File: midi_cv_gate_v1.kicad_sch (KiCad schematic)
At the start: 29 parts, among them J1 Conn_02x05_Odd_Even, J34 Conn_01x08, J35 Conn_01x08, J36 Conn_01x20, J37 Conn_01x20, J42 Conn_01x20, J43 Conn_01x20, U1 LM7805_TO220

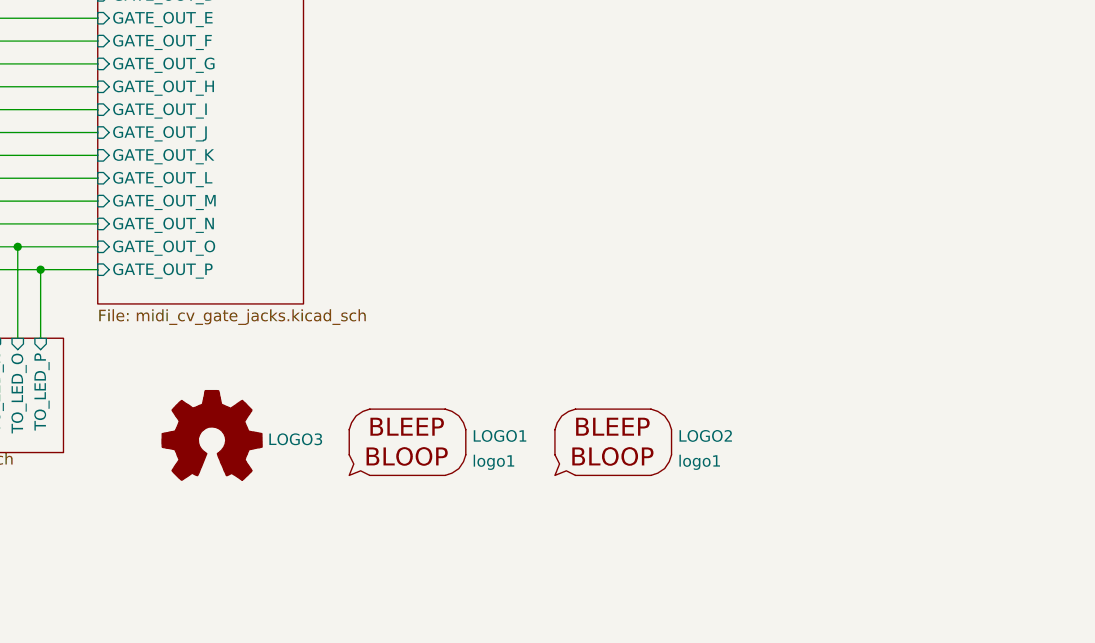
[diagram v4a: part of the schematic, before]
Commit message: First pass routing done, ERC passes, except interboard nets
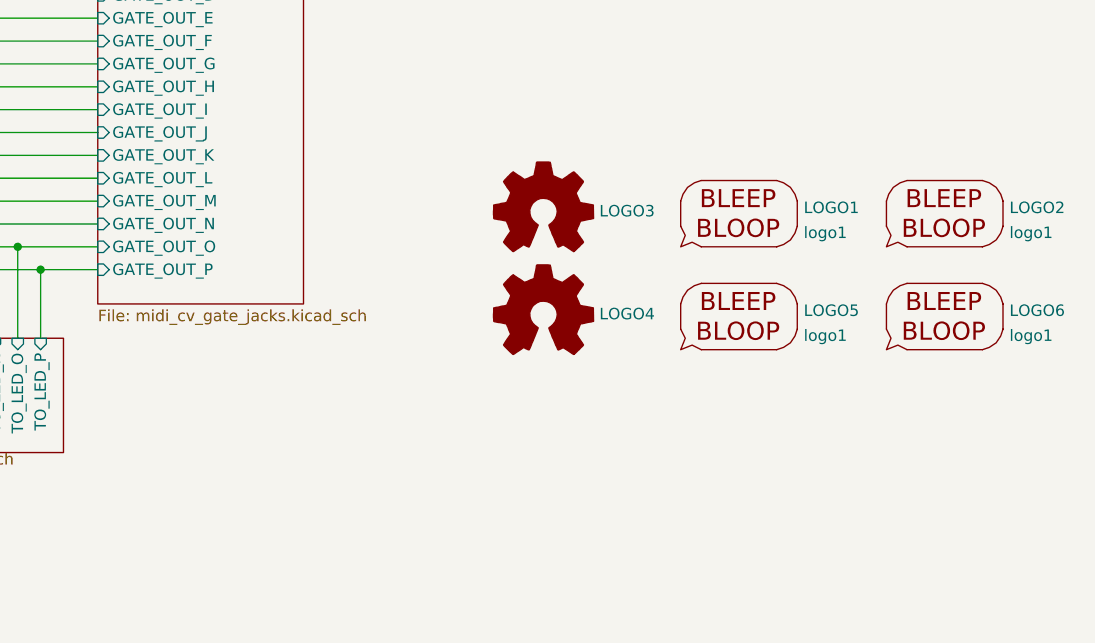
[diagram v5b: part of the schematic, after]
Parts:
- added LOGO4: Logo_Open_Hardware_Small, Symbol:OSHW-Symbol_6.7x6mm_SilkScreen, symbol My Stuff:Logo_Open_Hardware_Small
- added LOGO5: logo1, My Stuff:Logo1, symbol My Stuff:logo1
- added LOGO6: logo1, My Stuff:Logo2, symbol My Stuff:logo1
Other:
- moved on the sheet: LOGO1, LOGO2, LOGO3
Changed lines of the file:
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@@
     (pin "1")
   )
-  (symbol (lib_id "My Stuff:Logo_Open_Hardware_Small") (at 187.96 173.99 0) (unit 1)
-    (in_bom yes) (on_board yes) (fields_autoplaced)
-    (property "Reference" "LOGO3" (id 0) (at 194.1576 173.834 0)
-      (effects (font (size 1.27 1.27)) (justify left))
-    )
-    (property "Value" "Logo_Open_Hardware_Small" (id 1) (at 187.96 179.705 0)
-      (effects (font (size 1.27 1.27)) hide)
-    )
-    (property "Footprint" "Symbol:OSHW-Symbol_6.7x6mm_SilkScreen" (id 2) (at 187.96 173.99 0)
-      (effects (font (size 1.27 1.27)) hide)
-    )
-    (property "Datasheet" "~" (id 3) (at 187.96 173.99 0)
+  (symbol (lib_id "My Stuff:Logo_Open_Hardware_Small") (at 224.79 148.59 0) (unit 1)
+    (in_bom yes) (on_board yes) (fields_autoplaced)
+    (property "Reference" "LOGO3" (id 0) (at 230.9876 148.434 0)
+      (effects (font (size 1.27 1.27)) (justify left))
+    )
+    (property "Value" "Logo_Open_Hardware_Small" (id 1) (at 224.79 154.305 0)
+      (effects (font (size 1.27 1.27)) hide)
+    )
+    (property "Footprint" "Symbol:OSHW-Symbol_6.7x6mm_SilkScreen" (id 2) (at 224.79 148.59 0)
+      (effects (font (size 1.27 1.27)) hide)
+    )
+    (property "Datasheet" "~" (id 3) (at 224.79 148.59 0)
       (effects (font (size 1.27 1.27)) hide)
     )
@@
     (pin "2")
   )
-  (symbol (lib_id "My Stuff:logo1") (at 232.41 173.99 0) (unit 1)
-    (in_bom yes) (on_board yes) (fields_autoplaced)
-    (property "Reference" "LOGO2" (id 0) (at 239.7252 173.4625 0)
-      (effects (font (size 1.27 1.27)) (justify left))
-    )
-    (property "Value" "logo1" (id 1) (at 239.7252 176.2376 0)
-      (effects (font (size 1.27 1.27)) (justify left))
-    )
-    (property "Footprint" "My Stuff:Logo2" (id 2) (at 232.41 172.72 0)
-      (effects (font (size 1.27 1.27)) hide)
-    )
-    (property "Datasheet" "" (id 3) (at 232.41 172.72 0)
+  (symbol (lib_id "My Stuff:logo1") (at 269.24 148.59 0) (unit 1)
+    (in_bom yes) (on_board yes) (fields_autoplaced)
+    (property "Reference" "LOGO2" (id 0) (at 276.5552 148.0625 0)
+      (effects (font (size 1.27 1.27)) (justify left))
+    )
+    (property "Value" "logo1" (id 1) (at 276.5552 150.8376 0)
+      (effects (font (size 1.27 1.27)) (justify left))
+    )
+    (property "Footprint" "My Stuff:Logo2" (id 2) (at 269.24 147.32 0)
+      (effects (font (size 1.27 1.27)) hide)
+    )
+    (property "Datasheet" "" (id 3) (at 269.24 147.32 0)
       (effects (font (size 1.27 1.27)) hide)
     )
@@
     (pin "1")
   )
+  (symbol (lib_id "My Stuff:Logo_Open_Hardware_Small") (at 224.79 160.02 0) (unit 1)
+    (in_bom yes) (on_board yes) (fields_autoplaced)
+    (property "Reference" "LOGO4" (id 0) (at 230.9876 159.864 0)
+      (effects (font (size 1.27 1.27)) (justify left))
+    )
+    (property "Value" "Logo_Open_Hardware_Small" (id 1) (at 224.79 165.735 0)
+      (effects (font (size 1.27 1.27)) hide)
+    )
+    (property "Footprint" "Symbol:OSHW-Symbol_6.7x6mm_SilkScreen" (id 2) (at 224.79 160.02 0)
+      (effects (font (size 1.27 1.27)) hide)
+    )
+    (property "Datasheet" "~" (id 3) (at 224.79 160.02 0)
+      (effects (font (size 1.27 1.27)) hide)
+    )
+  )
   (symbol (lib_id "power:+12V") (at 154.94 40.64 180) (unit 1)
     (in_bom yes) (on_board yes)
@@
     )
     (pin "1")
+  )
+  (symbol (lib_id "My Stuff:logo1") (at 246.38 160.02 0) (unit 1)
+    (in_bom yes) (on_board yes) (fields_autoplaced)
+    (property "Reference" "LOGO5" (id 0) (at 253.6952 159.4925 0)
+      (effects (font (size 1.27 1.27)) (justify left))
+    )
+    (property "Value" "logo1" (id 1) (at 253.6952 162.2676 0)
+      (effects (font (size 1.27 1.27)) (justify left))
+    )
+    (property "Footprint" "My Stuff:Logo1" (id 2) (at 246.38 158.75 0)
+      (effects (font (size 1.27 1.27)) hide)
+    )
+    (property "Datasheet" "" (id 3) (at 246.38 158.75 0)
+      (effects (font (size 1.27 1.27)) hide)
+    )
   )
   (symbol (lib_id "power:-12VA") (at 81.28 29.845 90) (unit 1)
@@
     (pin "1")
   )
-  (symbol (lib_id "My Stuff:logo1") (at 209.55 173.99 0) (unit 1)
-    (in_bom yes) (on_board yes) (fields_autoplaced)
-    (property "Reference" "LOGO1" (id 0) (at 216.8652 173.4625 0)
-      (effects (font (size 1.27 1.27)) (justify left))
-    )
-    (property "Value" "logo1" (id 1) (at 216.8652 176.2376 0)
-      (effects (font (size 1.27 1.27)) (justify left))
-    )
-    (property "Footprint" "My Stuff:Logo1" (id 2) (at 209.55 172.72 0)
-      (effects (font (size 1.27 1.27)) hide)
-    )
-    (property "Datasheet" "" (id 3) (at 209.55 172.72 0)
+  (symbol (lib_id "My Stuff:logo1") (at 246.38 148.59 0) (unit 1)
+    (in_bom yes) (on_board yes) (fields_autoplaced)
+    (property "Reference" "LOGO1" (id 0) (at 253.6952 148.0625 0)
+      (effects (font (size 1.27 1.27)) (justify left))
+    )
+    (property "Value" "logo1" (id 1) (at 253.6952 150.8376 0)
+      (effects (font (size 1.27 1.27)) (justify left))
+    )
+    (property "Footprint" "My Stuff:Logo1" (id 2) (at 246.38 147.32 0)
+      (effects (font (size 1.27 1.27)) hide)
+    )
+    (property "Datasheet" "" (id 3) (at 246.38 147.32 0)
       (effects (font (size 1.27 1.27)) hide)
     )
@@
     )
     (pin "1")
+  )
+  (symbol (lib_id "My Stuff:logo1") (at 269.24 160.02 0) (unit 1)
+    (in_bom yes) (on_board yes) (fields_autoplaced)
+    (property "Reference" "LOGO6" (id 0) (at 276.5552 159.4925 0)
+      (effects (font (size 1.27 1.27)) (justify left))
+    )
+    (property "Value" "logo1" (id 1) (at 276.5552 162.2676 0)
+      (effects (font (size 1.27 1.27)) (justify left))
+    )
+    (property "Footprint" "My Stuff:Logo2" (id 2) (at 269.24 158.75 0)
+      (effects (font (size 1.27 1.27)) hide)
+    )
+    (property "Datasheet" "" (id 3) (at 269.24 158.75 0)
+      (effects (font (size 1.27 1.27)) hide)
+    )
   )
   (symbol (lib_id "Mechanical:MountingHole_Pad") (at 198.12 30.48 0) (unit 1)
@@
       (reference "LOGO3") (unit 1) (value "Logo_Open_Hardware_Small") (footprint "Symbol:OSHW-Symbol_6.7x6mm_SilkScreen")
     )
+    (path "/546f1e6f-02c3-4f3f-a3a2-a2915ddf3dbe"
+      (reference "LOGO4") (unit 1) (value "Logo_Open_Hardware_Small") (footprint "Symbol:OSHW-Symbol_6.7x6mm_SilkScreen")
+    )
+    (path "/6a3eb0bf-13cd-47e9-918c-e83f6facf8f2"
+      (reference "LOGO5") (unit 1) (value "logo1") (footprint "My Stuff:Logo1")
+    )
+    (path "/d6be7f74-368a-42ca-b4df-0b86bfe3c507"
+      (reference "LOGO6") (unit 1) (value "logo1") (footprint "My Stuff:Logo2")
+    )
     (path "/e0c84674-31e6-4d06-a99e-e9f0c7d90780/bee48c11-fcd3-4ece-9b9d-dca15f04a151"

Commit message: Fixed alignment of jacks and LEDs
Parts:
- renumbered C6 to C10, C5 to C101, C1 to C102, C4 to C103, C2 to C104, C3 to C105, D2 to D101, D3 to D102, FB1 to FB100, FB2 to FB101, H1 to H201, H5 to H202, H7 to H203, H3 to H204, H6 to H4, H8 to H6, H4 to H8, J1 to J101, J37 to J301, J43 to J302, J35 to J303, J42 to J34, J34 to J38, LOGO1 to LOGO201, LOGO2 to LOGO202, LOGO3 to LOGO203, LOGO6 to LOGO4, LOGO4 to LOGO6, U1 to U107

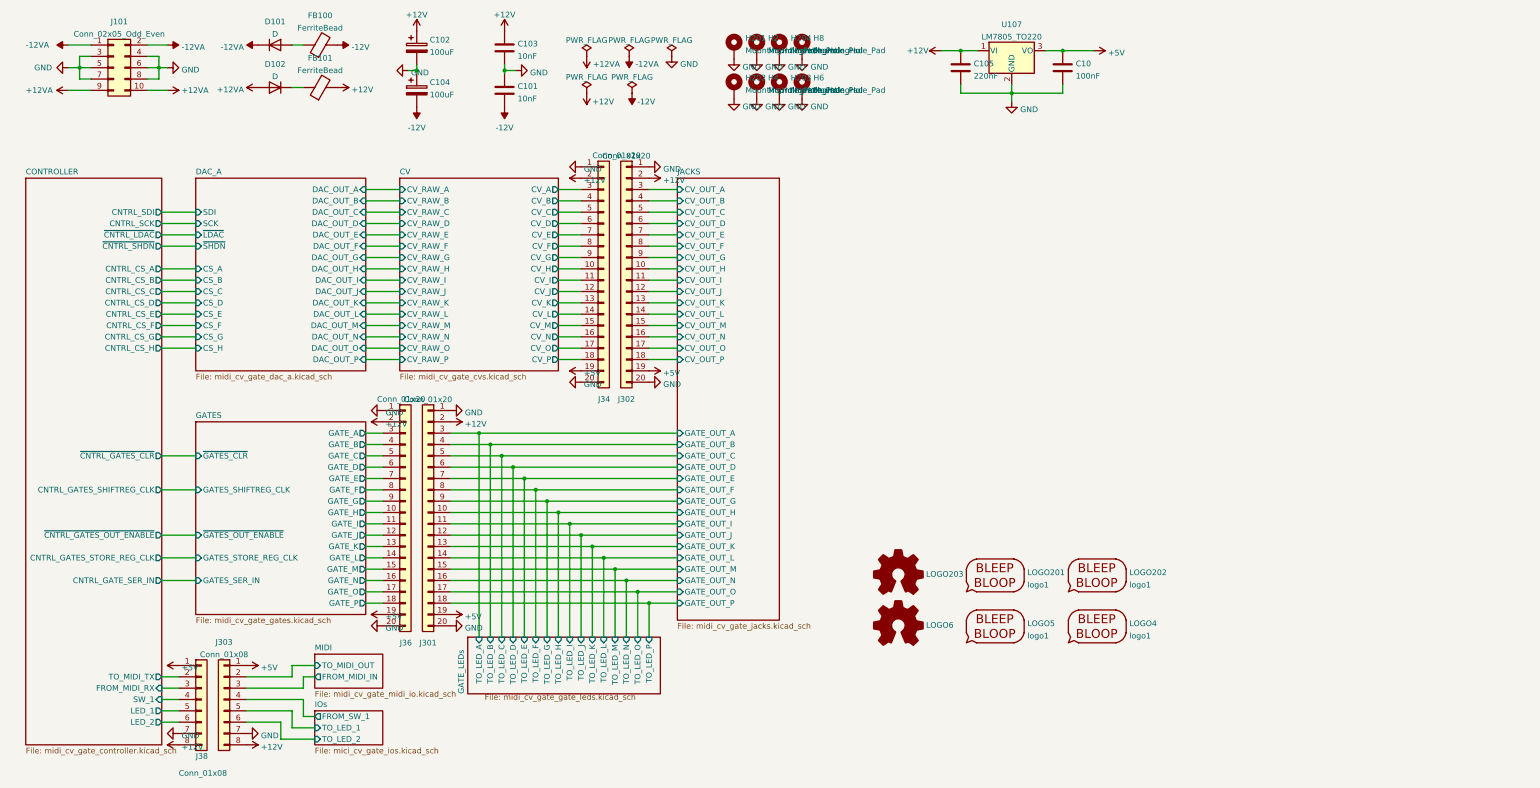
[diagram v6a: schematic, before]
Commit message: Cleanups and title blocks
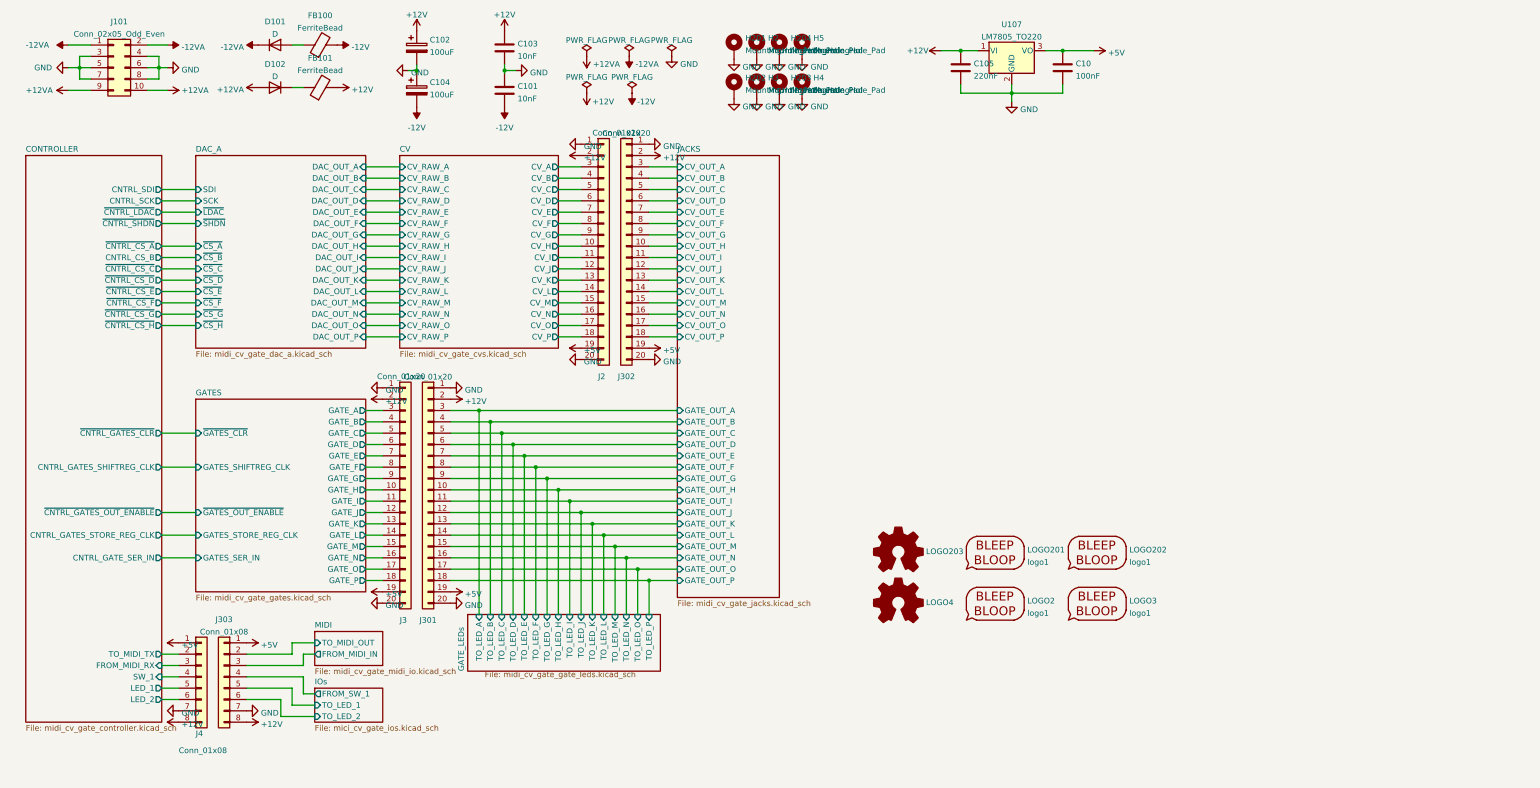
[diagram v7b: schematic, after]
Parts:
- renumbered H4 to H3, H6 to H4, H8 to H5, J34 to J2, J36 to J3, J38 to J4, LOGO5 to LOGO2, LOGO4 to LOGO3, LOGO6 to LOGO4
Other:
- sheet CONTROLLER ports: added ~{CNTRL_CS_A}, ~{CNTRL_CS_C}, ~{CNTRL_CS_D}, ~{CNTRL_CS_E}, ~{CNTRL_CS_F}, ~{CNTRL_CS_G}, ~{CNTRL_CS_H}, ~{}CNTRL_CS_B; removed CNTRL_CS_A, CNTRL_CS_B, CNTRL_CS_C, CNTRL_CS_D, CNTRL_CS_E, CNTRL_CS_F, CNTRL_CS_G, CNTRL_CS_H
- sheet DAC_A ports: added ~{CS_A}, ~{CS_B}, ~{CS_C}, ~{CS_D}, ~{CS_E}, ~{CS_F}, ~{CS_G}, ~{CS_H}; removed CS_A, CS_B, CS_C, CS_D, CS_E, CS_F, CS_G, CS_H
- company: (none) -> RobotDialogs
- title: (none) -> Eurorack MIDI 16x16 CV Gate
- moved on the sheet: J2, J3, J301, J302, J303, J4, LOGO2, LOGO201, LOGO202, LOGO203, LOGO3, LOGO4
